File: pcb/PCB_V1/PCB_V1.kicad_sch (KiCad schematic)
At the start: 13 parts, among them U101 TPS54202DDCR

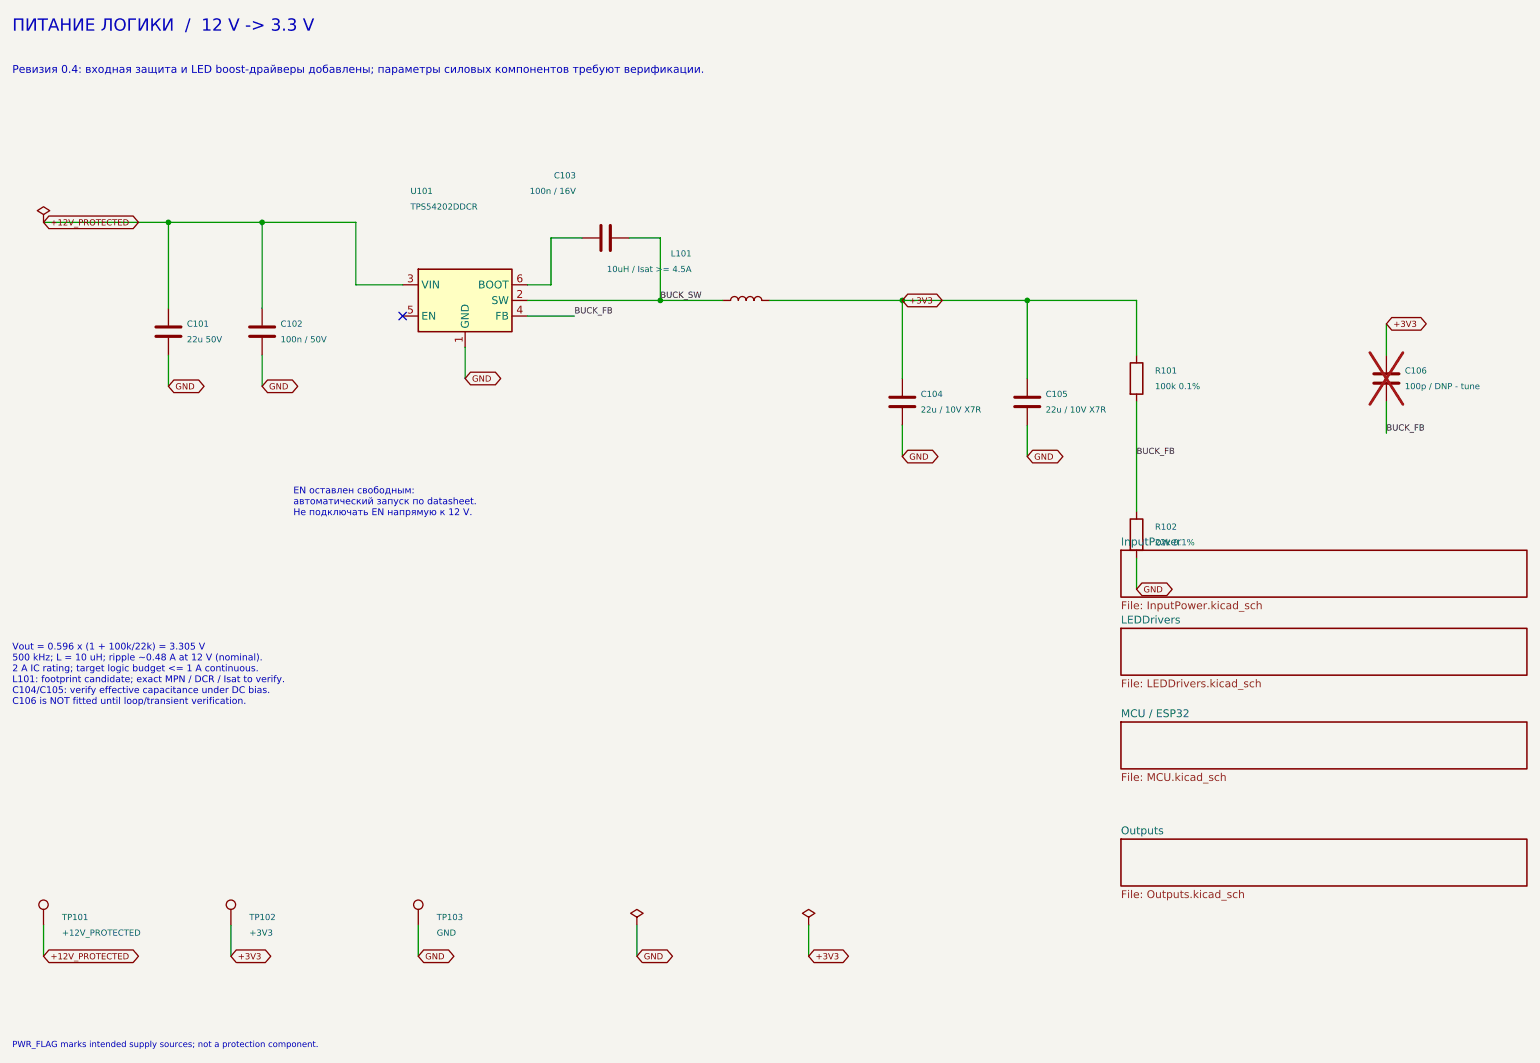
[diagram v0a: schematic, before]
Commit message: pcb: move board to 24 V input with 12 V aux buck and merged LED bar channel
Revision 0.14 of PCB_V1 (see pcb/PCB_V1/REDESIGN_24V.md):
- 24 V input on keyed XT60PW-M (pin 1 GND, pin 2 +24V); LM74700, input
  MOSFET and F901 removed; SMBJ26CA TVS; 220 uF/50 V bulk
- ATM mini-blade fuses in XF-508P-B-B holders: F902 10 A loads, F903 7.5 A LED
- new LMR16020 24 V -> 12 V aux buck (500 kHz) feeding PC fans, the
  UCC27524A heater gate driver and the TPS54202 3.3 V buck; TPS70950 removed
- heater and pump on 24 V: SMBJ30A drain TVS, AO3422 + SS36 pump stage
- LED CH1 panel keeps SRP1770TA/0.027 R/1k, switch now CSD19534Q5A;
  CH2 drives both identical bars in parallel (J721 || J731, 0.40 R);
  third AL8853 channel removed
- TS-1187A buttons, DORABO/KANGNEX terminals
- project library: LMR16020 and CSD19534Q5A symbols, TI DQJ and XF-508P
  footprints
- verify_netlist.py / verify_board.py / analyze_*.py updated for 24 V;
  new sync_board.py updates the unrouted staging board from the netlist
- ERC 0/0; netlist, board and sizing checks pass; DRC only the 12 known
  ESP32 drill sizes plus unrouted connections; 163 components

Co-Authored-By: Claude Opus 5.5 <noreply@anthropic.com>
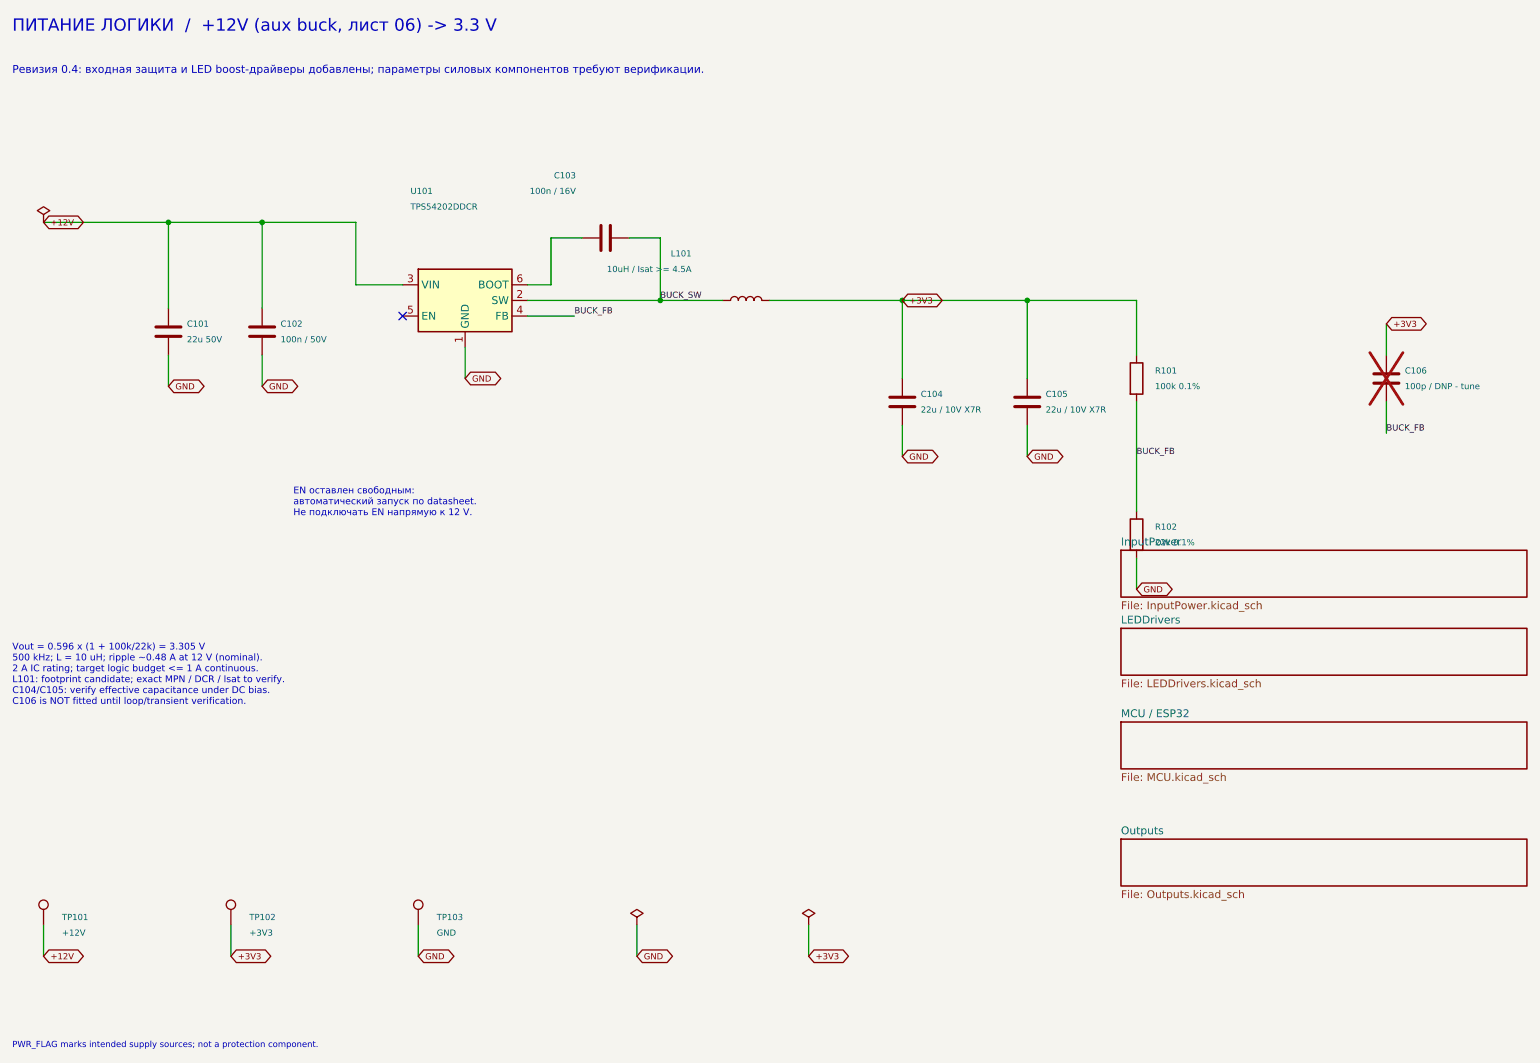
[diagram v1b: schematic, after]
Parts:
- TP101: value +12V_PROTECTED -> +12V
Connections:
- net +12V_PROTECTED renamed +12V
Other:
- note added: "ПИТАНИЕ ЛОГИКИ / +12V (aux buck, лист 06) -> 3.3 V"
- note removed: "ПИТАНИЕ ЛОГИКИ / 12 V -> 3.3 V"
- title: 01 - Logic power / 12 V to 3.3 V -> 01 - Logic power / 12 V aux to 3.3 V
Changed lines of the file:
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@@
 	(paper "A4")
 	(title_block
-		(title "01 - Logic power / 12 V to 3.3 V")
-		(date "2026-09-26")
-		(rev "0.4-DRAFT")
+		(title "01 - Logic power / 12 V aux to 3.3 V")
+		(date "2026-09-27")
+		(rev "0.14-DRAFT")
 		(company "GrowBox controller")
 		(comment 1 "Draft: input protection and LED drivers pending")
@@
 		)
 	)
-	(text "ПИТАНИЕ ЛОГИКИ  /  12 V -> 3.3 V"
+	(text "ПИТАНИЕ ЛОГИКИ  /  +12V (aux buck, лист 06) -> 3.3 V"
 		(exclude_from_sim no)
 		(at 20.32 17.78 0)
@@
 		)
 	)
-	(global_label "+12V_PROTECTED"
+	(global_label "+12V"
 		(shape bidirectional)
 		(at 25.4 170.18 0)
@@
 		)
 	)
-	(global_label "+12V_PROTECTED"
+	(global_label "+12V"
 		(shape bidirectional)
 		(at 25.4 50.8 0)
@@
 			)
 		)
-		(property "Value" "+12V_PROTECTED"
+		(property "Value" "+12V"
 			(at 28.4 166.37 0)
 			(show_name no)
